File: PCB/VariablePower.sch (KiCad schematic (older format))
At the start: 18 parts, among them U10 LT3080, U11 LT3080

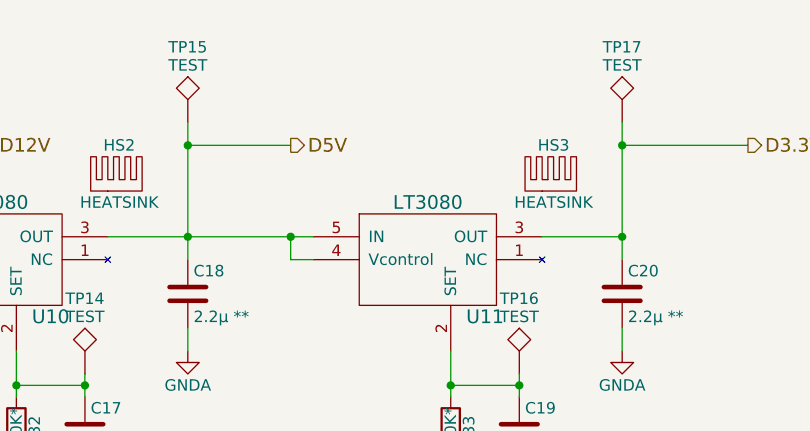
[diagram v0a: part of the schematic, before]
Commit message: component layout done
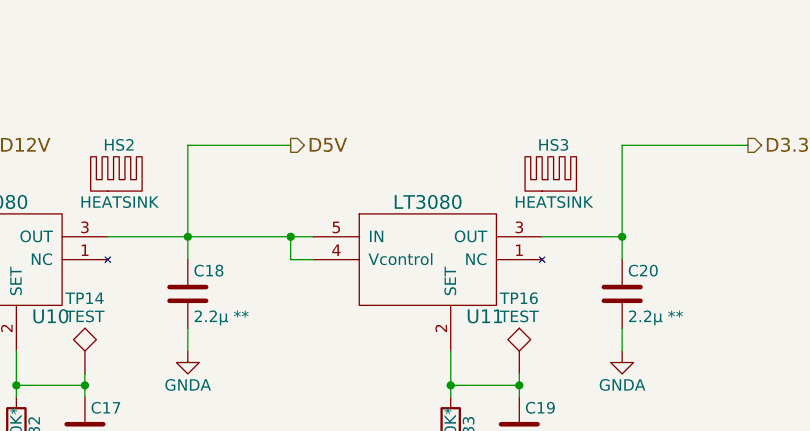
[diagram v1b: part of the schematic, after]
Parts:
- removed TP15, TP17: TEST, Measurement_Points:Measurement_Point_Round-SMD-Pad_Small, symbol TEST
- C17, C18, C19, C20: footprint Capacitors_Tantalum_SMD:CP_Tantalum_Case-B_EIA-3528-21_Hand -> Capacitors_Tantalum_SMD:CP_Tantalum_Case-A_EIA-3216-18_Reflow
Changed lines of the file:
@@
 	4000 3650 4000 3750
-$Comp
-L TEST TP15
-U 1 1 5932C638
-P 4750 2150
-F 0 "TP15" H 4750 2450 50  0000 C BNN
-F 1 "TEST" H 4750 2400 50  0000 C CNN
-F 2 "Measurement_Points:Measurement_Point_Round-SMD-Pad_Small" H 4750 2150 50  0001 C CNN
-F 3 "" H 4750 2150 50  0000 C CNN
-	1    4750 2150
-	1    0    0    -1
-$EndComp
 $Comp
 L C C17
@@
 F 0 "C17" H 4325 3600 50  0000 L CNN
 F 1 "1µ**" H 4325 3400 50  0000 L CNN
-F 2 "Capacitors_Tantalum_SMD:CP_Tantalum_Case-B_EIA-3528-21_Hand" H 4338 3350 50  0001 C CNN
+F 2 "Capacitors_Tantalum_SMD:CP_Tantalum_Case-A_EIA-3216-18_Reflow" H 4338 3350 50  0001 C CNN
 F 3 "" H 4300 3500 50  0000 C CNN
 	1    4300 3500
@@
 F 0 "C18" H 4775 3000 50  0000 L CNN
 F 1 "2.2µ **" H 4775 2800 50  0000 L CNN
-F 2 "Capacitors_Tantalum_SMD:CP_Tantalum_Case-B_EIA-3528-21_Hand" H 4788 2750 50  0001 C CNN
+F 2 "Capacitors_Tantalum_SMD:CP_Tantalum_Case-A_EIA-3216-18_Reflow" H 4788 2750 50  0001 C CNN
 F 3 "" H 4750 2900 50  0000 C CNN
 	1    4750 2900
@@
 	4400 2650 5300 2650
 Wire Wire Line
-	4750 2150 4750 2750
-Wire Wire Line
 	4750 2250 5200 2250
-Connection ~ 4750 2250
 Connection ~ 4750 2650
 Wire Wire Line
@@
 F 0 "C19" H 6225 3600 50  0000 L CNN
 F 1 "1µ**" H 6225 3400 50  0000 L CNN
-F 2 "Capacitors_Tantalum_SMD:CP_Tantalum_Case-B_EIA-3528-21_Hand" H 6238 3350 50  0001 C CNN
+F 2 "Capacitors_Tantalum_SMD:CP_Tantalum_Case-A_EIA-3216-18_Reflow" H 6238 3350 50  0001 C CNN
 F 3 "" H 6200 3500 50  0000 C CNN
 	1    6200 3500
@@
 F 0 "C20" H 6675 3000 50  0000 L CNN
 F 1 "2.2µ **" H 6675 2800 50  0000 L CNN
-F 2 "Capacitors_Tantalum_SMD:CP_Tantalum_Case-B_EIA-3528-21_Hand" H 6688 2750 50  0001 C CNN
+F 2 "Capacitors_Tantalum_SMD:CP_Tantalum_Case-A_EIA-3216-18_Reflow" H 6688 2750 50  0001 C CNN
 F 3 "" H 6650 2900 50  0000 C CNN
 	1    6650 2900
@@
 Wire Wire Line
 	6650 2650 6300 2650
-Wire Wire Line
-	6650 2150 6650 2750
 Connection ~ 6650 2650
 Wire Wire Line
@@
 	5200 2750 5200 2650
 Connection ~ 5200 2650
-$Comp
-L TEST TP17
-U 1 1 5932D69A
-P 6650 2150
-F 0 "TP17" H 6650 2450 50  0000 C BNN
-F 1 "TEST" H 6650 2400 50  0000 C CNN
-F 2 "Measurement_Points:Measurement_Point_Round-SMD-Pad_Small" H 6650 2150 50  0001 C CNN
-F 3 "" H 6650 2150 50  0000 C CNN
-	1    6650 2150
-	1    0    0    -1
-$EndComp
 Wire Wire Line
 	6650 2250 7200 2250
-Connection ~ 6650 2250
 Text Notes 3550 4350 0    60   ~ 0
 10µA ( intern currtent source) \nx\n500K resistor \n= 5V Set Pin
@@
 $EndComp
 $Comp
-L GNDA #PWR047
+L GNDA #PWR050
 U 1 1 59361100
 P 1800 2550
-F 0 "#PWR047" H 1800 2300 50  0001 C CNN
+F 0 "#PWR050" H 1800 2300 50  0001 C CNN
 F 1 "GNDA" H 1800 2400 50  0000 C CNN
 F 2 "" H 1800 2550 50  0000 C CNN
@@
 $EndComp
 $Comp
-L GNDA #PWR048
+L GNDA #PWR051
 U 1 1 59361244
 P 2250 2800
-F 0 "#PWR048" H 2250 2550 50  0001 C CNN
+F 0 "#PWR051" H 2250 2550 50  0001 C CNN
 F 1 "GNDA" H 2250 2650 50  0000 C CNN
 F 2 "" H 2250 2800 50  0000 C CNN
@@
 $EndComp
 $Comp
-L GNDA #PWR049
+L GNDA #PWR052
 U 1 1 59361285
 P 2700 2800
-F 0 "#PWR049" H 2700 2550 50  0001 C CNN
+F 0 "#PWR052" H 2700 2550 50  0001 C CNN
 F 1 "GNDA" H 2700 2650 50  0000 C CNN
 F 2 "" H 2700 2800 50  0000 C CNN
@@
 $EndComp
 $Comp
-L GNDA #PWR050
+L GNDA #PWR053
 U 1 1 59361488
 P 4000 3750
-F 0 "#PWR050" H 4000 3500 50  0001 C CNN
+F 0 "#PWR053" H 4000 3500 50  0001 C CNN
 F 1 "GNDA" H 4000 3600 50  0000 C CNN
 F 2 "" H 4000 3750 50  0000 C CNN
@@
 $EndComp
 $Comp
-L GNDA #PWR051
+L GNDA #PWR054
 U 1 1 59361679
 P 4300 3750
-F 0 "#PWR051" H 4300 3500 50  0001 C CNN
+F 0 "#PWR054" H 4300 3500 50  0001 C CNN
 F 1 "GNDA" H 4300 3600 50  0000 C CNN
 F 2 "" H 4300 3750 50  0000 C CNN
@@
 $EndComp
 $Comp
-L GNDA #PWR052
+L GNDA #PWR055
 U 1 1 593616BA
 P 5900 3750
-F 0 "#PWR052" H 5900 3500 50  0001 C CNN
+F 0 "#PWR055" H 5900 3500 50  0001 C CNN
 F 1 "GNDA" H 5900 3600 50  0000 C CNN
 F 2 "" H 5900 3750 50  0000 C CNN
@@
 $EndComp
 $Comp
-L GNDA #PWR053
+L GNDA #PWR056
 U 1 1 593618AB
 P 6200 3750
-F 0 "#PWR053" H 6200 3500 50  0001 C CNN
+F 0 "#PWR056" H 6200 3500 50  0001 C CNN
 F 1 "GNDA" H 6200 3600 50  0000 C CNN
 F 2 "" H 6200 3750 50  0000 C CNN
@@
 $EndComp
 $Comp
-L GNDA #PWR054
+L GNDA #PWR057
 U 1 1 59361958
 P 6650 3150
-F 0 "#PWR054" H 6650 2900 50  0001 C CNN
+F 0 "#PWR057" H 6650 2900 50  0001 C CNN
 F 1 "GNDA" H 6650 3000 50  0000 C CNN
 F 2 "" H 6650 3150 50  0000 C CNN
@@
 $EndComp
 $Comp
-L GNDA #PWR055
+L GNDA #PWR058
 U 1 1 59361B5B
 P 4750 3150
-F 0 "#PWR055" H 4750 2900 50  0001 C CNN
+F 0 "#PWR058" H 4750 2900 50  0001 C CNN
 F 1 "GNDA" H 4750 3000 50  0000 C CNN
 F 2 "" H 4750 3150 50  0000 C CNN
@@
 	1    0    0    -1
 $EndComp
+Wire Wire Line
+	4750 2250 4750 2750
+Wire Wire Line
+	6650 2250 6650 2750
 $EndSCHEMATC
